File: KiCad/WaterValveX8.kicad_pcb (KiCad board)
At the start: 2 copper layers, 63.2 x 39.1 mm, 50 parts, among them J1 Conn_01x04_Male, J2 Barrel_Jack, J3 Conn_01x03_Male, J4 Conn_01x01_Male, J5 Conn_01x04_Male, J6 Screw_Terminal_01x03, J7 Screw_Terminal_01x03, J8 Screw_Terminal_01x03, J9 Screw_Terminal_01x02, Q1 IRLML2502, Q2 IRLML2502, Q3 IRLML2502, Q4 IRLML2502, U1 Project_DCDC_01, U2 SeedStudio XIAO ESP32 C3 v1, U3 L7805

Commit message: First X8 layout
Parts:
- removed J1: Conn_01x04_Male, Connector_PinHeader_2.54mm:PinHeader_1x04_P2.54mm_Vertical
- removed U1: Project_DCDC_01, LOCAL1:DCDC_01
- added D13: LED, LED_SMD:LED_0805_2012Metric_Pad1.15x1.40mm_HandSolder, F.Cu at (186.5, 86.6)
- added D14: LED, LED_THT:LED_D3.0mm, B.Cu at (177.8, 94.0)
- added D15: LED, LED_THT:LED_D3.0mm, B.Cu at (192.8, 113.2)
- added D16: LED, LED_THT:LED_D3.0mm, B.Cu at (192.8, 108.0)
- added D17: LED, LED_THT:LED_D3.0mm, B.Cu at (192.9, 102.5)
- added D18: LED, LED_THT:LED_D3.0mm, B.Cu at (192.8, 96.8)
- added D19: LED, LED_THT:LED_D3.0mm, B.Cu at (152.4, 112.5)
- added D20: LED, LED_SMD:LED_0805_2012Metric_Pad1.15x1.40mm_HandSolder, F.Cu at (151.1, 112.5)
- added D21: 1N4148, Diode_SMD:D_MiniMELF, F.Cu at (147.2, 113.0)
- added D22: LED, LED_THT:LED_D3.0mm, B.Cu at (152.4, 106.4)
- added D23: LED, LED_SMD:LED_0805_2012Metric_Pad1.15x1.40mm_HandSolder, F.Cu at (151.1, 106.4)
- added D24: 1N4148, Diode_SMD:D_MiniMELF, F.Cu at (147.2, 107.0)
- added D25: LED, LED_THT:LED_D3.0mm, B.Cu at (152.4, 100.6)
- added D26: LED, LED_SMD:LED_0805_2012Metric_Pad1.15x1.40mm_HandSolder, F.Cu at (151.1, 100.6)
- added D27: 1N4148, Diode_SMD:D_MiniMELF, F.Cu at (147.2, 101.0)
- added D28: LED, LED_THT:LED_D3.0mm, B.Cu at (152.4, 94.7)
- added D29: LED, LED_SMD:LED_0805_2012Metric_Pad1.15x1.40mm_HandSolder, F.Cu at (151.1, 94.7)
- added D30: 1N4148, Diode_SMD:D_MiniMELF, F.Cu at (147.2, 95.2)
- added J10: Screw_Terminal_01x03, TerminalBlock_Phoenix:TerminalBlock_Phoenix_PT-1,5-3-3.5-H_1x03_P3.50mm_Horizontal, F.Cu at (142.3, 106.8)
- added J11: Conn_01x03_Pin, Connector_PinHeader_2.54mm:PinHeader_1x03_P2.54mm_Vertical, F.Cu at (147.5, 90.0)
- added Q5: IRLML2502, Package_TO_SOT_SMD:SOT-23_Handsoldering, F.Cu at (156.5, 115.6)
- added Q6: IRLML2502, Package_TO_SOT_SMD:SOT-23_Handsoldering, F.Cu at (156.5, 109.5)
- added Q7: IRLML2502, Package_TO_SOT_SMD:SOT-23_Handsoldering, F.Cu at (156.5, 103.4)
- added Q8: IRLML2502, Package_TO_SOT_SMD:SOT-23_Handsoldering, F.Cu at (156.5, 97.5)
- added R14: 1k, Resistor_SMD:R_0805_2012Metric_Pad1.20x1.40mm_HandSolder, F.Cu at (160.5, 115.6)
- added R17: 1k, Resistor_SMD:R_0805_2012Metric_Pad1.20x1.40mm_HandSolder, F.Cu at (155.7, 112.5)
- added R18: 1k, Resistor_SMD:R_0805_2012Metric_Pad1.20x1.40mm_HandSolder, F.Cu at (160.5, 109.5)
- added R19: 1k, Resistor_SMD:R_0805_2012Metric_Pad1.20x1.40mm_HandSolder, F.Cu at (155.7, 106.4)
- added R20: 1k, Resistor_SMD:R_0805_2012Metric_Pad1.20x1.40mm_HandSolder, F.Cu at (160.5, 103.5)
- added R21: 1k, Resistor_SMD:R_0805_2012Metric_Pad1.20x1.40mm_HandSolder, F.Cu at (155.7, 100.3)
- added R22: 1k, Resistor_SMD:R_0805_2012Metric_Pad1.20x1.40mm_HandSolder, F.Cu at (160.5, 97.5)
- added R23: 1k, Resistor_SMD:R_0805_2012Metric_Pad1.20x1.40mm_HandSolder, F.Cu at (155.7, 94.7)
- C1, C3: footprint Capacitor_Tantalum_SMD:CP_EIA-3216-18_Kemet-A_Pad1.58x1.35mm_HandSolder -> Capacitor_SMD:C_1206_3216Metric_Pad1.33x1.80mm_HandSolder
- D10, D3, D5, D8: moved to F.Cu
- D11: footprint LED_SMD:LED_0805_2012Metric_Pad1.15x1.40mm_HandSolder -> LED_THT:LED_D3.0mm; moved to B.Cu
- D12, D4, D6, D9: value 1N4007 -> 1N4148; footprint Diode_THT:D_DO-41_SOD81_P3.81mm_Vertical_KathodeUp -> Diode_SMD:D_MiniMELF
- J2: value Barrel_Jack -> Screw_Terminal_01x03; footprint LOCAL1:BarrelJack1 -> TerminalBlock_Phoenix:TerminalBlock_Phoenix_PT-1,5-3-3.5-H_1x03_P3.50mm_Horizontal
- U2: value SeedStudio XIAO ESP32 C3 v1 -> XIAO-ESP32-C6-SMD; footprint LOCAL1:XIAO_ESP32C3_THT -> LOCAL1:XIAO-ESP32-C6-SMD
- moved J9 32.6 mm to (160.2, 90.1), turned to 180 degrees
- moved J5 26.9 mm to (154.8, 119.2), turned to -90 degrees
- moved R5 24.2 mm to (151.0, 116.5), turned to 0 degrees
- moved R4 19.1 mm to (159.0, 119.2), turned to 180 degrees
- moved C2 15.7 mm to (166.1, 95.8)
- moved D12 14.0 mm to (198.0, 97.2), turned to -90 degrees
- moved C1 13.8 mm to (163.8, 95.2), turned to -90 degrees
- moved D9 13.7 mm to (197.9, 102.8), turned to -90 degrees
- moved D4 13.6 mm to (198.0, 114.2), turned to -90 degrees
- moved D6 13.5 mm to (197.9, 108.5), turned to -90 degrees
- moved J2 13.1 mm to (142.2, 95.0), turned to -90 degrees
- moved D10 12.8 mm to (193.8, 96.8), turned to 0 degrees
- moved D8 12.7 mm to (194.1, 102.5), turned to 0 degrees
- moved D11 12.6 mm to (187.7, 86.6)
- moved D5 12.4 mm to (194.0, 108.0), turned to 0 degrees
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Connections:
- D7 pad 2: /GPIO10 -> /D10
- J2 pad 1: /PwrIn -> +VSW
- J2 pad 2: GND -> /Relay8
- J2 pad 3: unconnected-(J2-Pad3) -> /Relay7
- R11 pad 1: /GPIO8 -> /D8
- R12 pad 2: /GPIO10 -> /D10
- R6 pad 1: /GPIO1 -> /D1
- R8 pad 1: /GPIO5 -> /D2
- R9 pad 1: /GPIO3 -> /D3
- U2 pad 1: /GPIO2 -> +5V
- U2 pad 10: Net-(D1-K) -> /SDA
- U2 pad 11: /GPIO10 -> /D3
- U2 pad 12: +3V3 -> /D2
- U2 pad 13: GND -> /D1
- U2 pad 14: +5V -> /GPIO2
- U2 pad 2: /GPIO1 -> GND
- U2 pad 3: /GPIO5 -> +3V3
- U2 pad 4: /GPIO3 -> /D10
- U2 pad 5: /SDA -> Net-(D1-K)
- U2 pad 6: /SCL -> /D8
- U2 pad 7: /TX -> /RX
- U2 pad 8: /RX -> /TX
- U2 pad 9: /GPIO8 -> /SCL
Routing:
- net +VSW: track 56.3 -> 148.1 mm
- net GND: track 0.00 -> 85.4 mm, vias 3 -> 12
- net /RX: track 3.25 -> 43.4 mm, vias 0 -> 2
- net /GPIO10: track 30.0 -> 0.00 mm, vias 1 -> 0
- net /PwrIn: track 55.8 -> 28.9 mm
- net /D3: track 0.00 -> 25.7 mm, vias 0 -> 2
- net /D1: track 0.00 -> 23.4 mm, vias 0 -> 2
- net /D2: track 0.00 -> 23.0 mm, vias 0 -> 2
- net +5V: track 85.6 -> 63.5 mm, vias 0 -> 1
- net /GPIO8: track 21.3 -> 0.00 mm, vias 1 -> 0
- net /D10: track 0.00 -> 19.9 mm, vias 0 -> 2
- net /Relay6: track 0.00 -> 19.2 mm
- net /Relay5: track 0.00 -> 18.3 mm
- net /Relay7: track 0.00 -> 16.9 mm
- net /Relay8: track 0.00 -> 16.8 mm
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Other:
- board size 63.2 x 39.1 mm -> 72.9 x 41.6 mm
- board text added: "(C) 2025 Hans Rune Bue <email@hansrune.net>"
- board text added: "GND 3V DA CL"
- board text added: "RX TX GND"
- board text added: "WaterValveX8 - Rev 4.0"
- board text removed: "(C) 2023 Hans Rune Bue <email@hansrune.net>"
- board text removed: "CL DA +3V GND"
- board text removed: "WaterValveX4 - Rev 2.0.1"

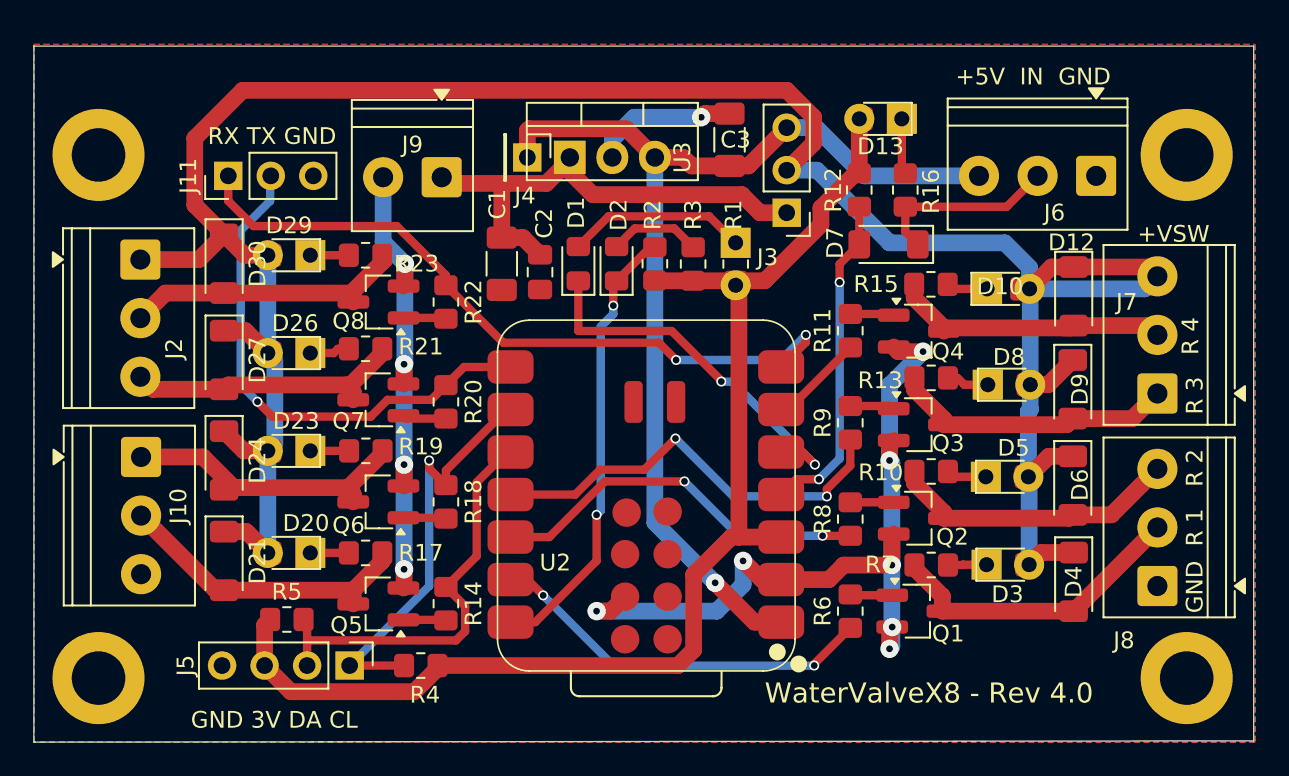
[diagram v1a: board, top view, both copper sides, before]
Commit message: Diode footprint changes
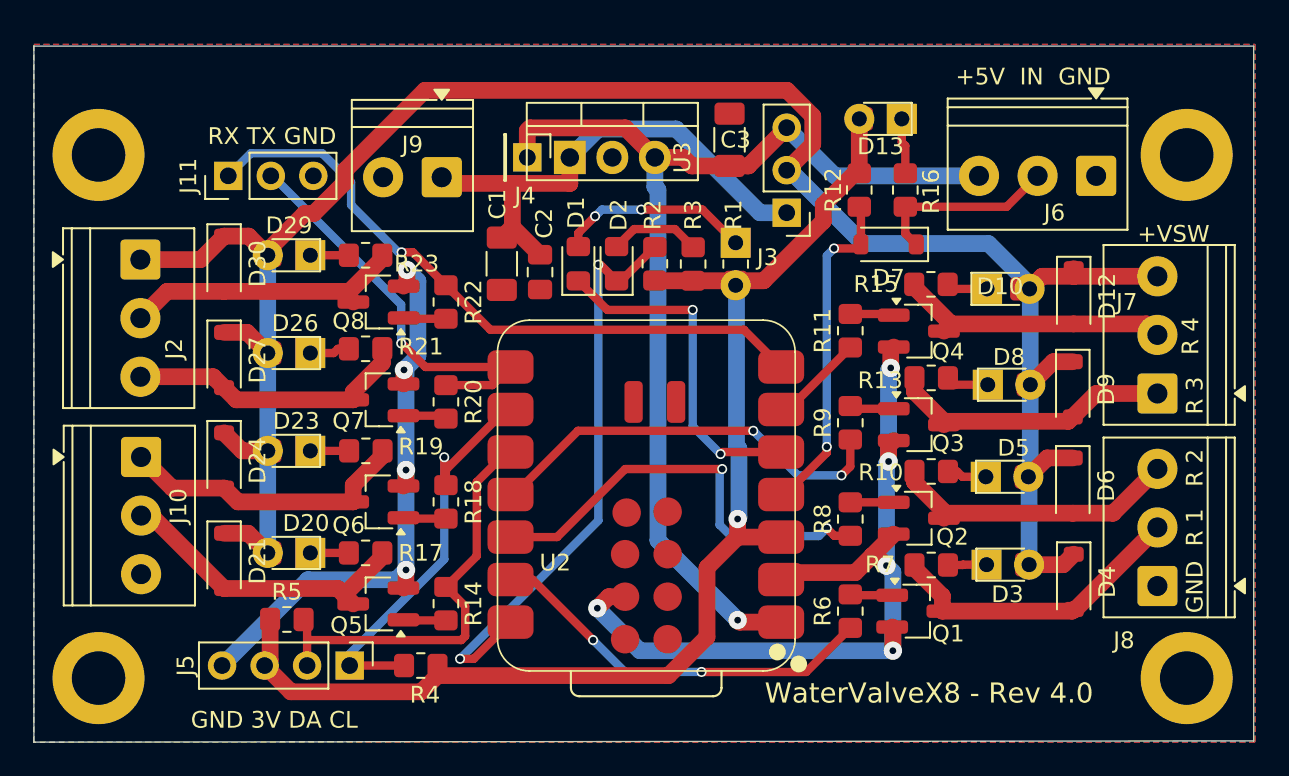
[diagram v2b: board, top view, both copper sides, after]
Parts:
- D12, D21, D24, D27, D30, D4, D6, D7, D9: footprint Diode_SMD:D_MiniMELF -> Diode_SMD:D_SOD-123
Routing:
- net +VSW: track 148.1 -> 131.4 mm
- net /GPIO2: track 27.0 -> 35.5 mm
- net /TX: track 31.4 -> 24.7 mm
- net /RX: track 43.4 -> 39.7 mm, vias 2 -> 1
- net /D2: track 23.0 -> 26.2 mm
- net Net-(D1-K): track 22.8 -> 20.5 mm
- net /PwrIn: track 28.9 -> 30.9 mm
- net GND: track 85.4 -> 87.1 mm, vias 12 -> 9
- net /Relay6: track 19.2 -> 17.6 mm
- net /D3: track 25.7 -> 24.8 mm
- net Net-(D1-A): track 11.1 -> 11.9 mm, vias 0 -> 2
- net +5V: track 63.5 -> 64.1 mm
- net +3V3: vias 0 -> 1

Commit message: Changed to combined C3/C6 and step-down PSU
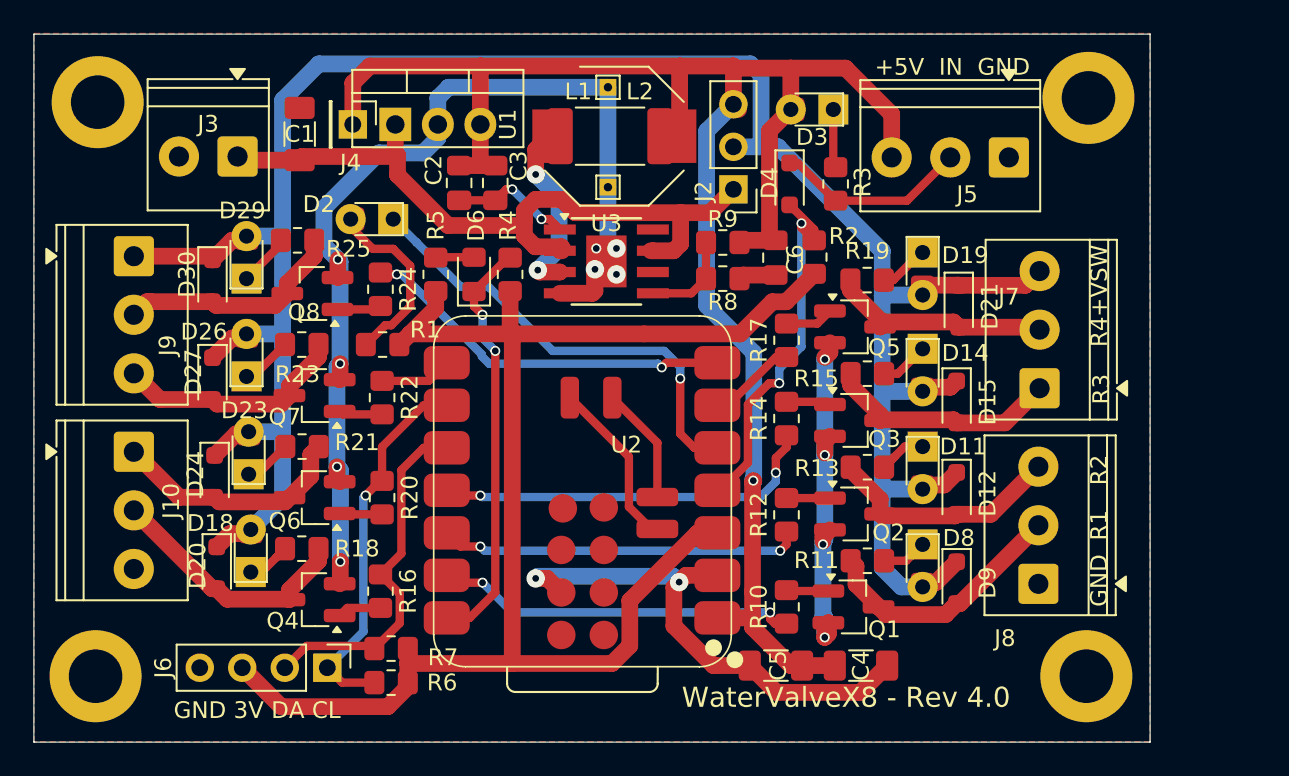
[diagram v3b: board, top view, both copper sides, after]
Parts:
- removed J11: Conn_01x03_Pin, Connector_PinHeader_2.54mm:PinHeader_1x03_P2.54mm_Vertical
- added C4: 22uF, Capacitor_SMD:C_1206_3216Metric_Pad1.33x1.80mm_HandSolder, F.Cu at (185.3, 119.3)
- added C5: 22uF, Capacitor_SMD:C_1206_3216Metric_Pad1.33x1.80mm_HandSolder, F.Cu at (180.2, 119.3)
- added C6: 100nF, Capacitor_SMD:C_0805_2012Metric_Pad1.18x1.45mm_HandSolder, F.Cu at (180.2, 94.9)
- added L1: L, Inductor_SMD:L_Bourns-SRU8028_8.0x8.0mm, F.Cu at (170.6, 87.6)
- added L2: L, Inductor_SMD:L_2512_6332Metric_Pad1.52x3.35mm_HandSolder, F.Cu at (170.3, 87.6)
- added R8: 88k7, Resistor_SMD:R_0805_2012Metric_Pad1.20x1.40mm_HandSolder, F.Cu at (177.0, 94.0)
- added R9: 20k, Resistor_SMD:R_0805_2012Metric_Pad1.20x1.40mm_HandSolder, F.Cu at (177.0, 96.1)
- added TP1: TestPoint, TestPoint:TestPoint_THTPad_1.0x1.0mm_Drill0.5mm, F.Cu at (170.2, 84.7)
- added TP2: TestPoint, TestPoint:TestPoint_THTPad_1.0x1.0mm_Drill0.5mm, F.Cu at (170.2, 90.7)
- added U3: MT2499A, Package_SO:TI_SO-PowerPAD-8, F.Cu at (170.1, 95.1)
- C1: value 10uF -> 22uF
- C3: value 10uF -> 22nF; footprint Capacitor_SMD:C_1206_3216Metric_Pad1.33x1.80mm_HandSolder -> Capacitor_SMD:C_0805_2012Metric_Pad1.18x1.45mm_HandSolder
- D12: renamed from D6; value 1N4148 -> 1N4007; footprint Diode_SMD:D_SOD-123 -> Diode_SMD:D_SOD-323_HandSoldering
- D15: renamed from D9; value 1N4148 -> 1N4007; footprint Diode_SMD:D_SOD-123 -> Diode_SMD:D_SOD-323_HandSoldering
- D20: renamed from D21; value 1N4148 -> 1N4007; footprint Diode_SMD:D_SOD-123 -> Diode_SMD:D_SOD-323_HandSoldering
- D21: renamed from D12; value 1N4148 -> 1N4007; footprint Diode_SMD:D_SOD-123 -> Diode_SMD:D_SOD-323_HandSoldering
- D24, D27, D30: value 1N4148 -> 1N4007; footprint Diode_SMD:D_SOD-123 -> Diode_SMD:D_SOD-323_HandSoldering
- D4: renamed from D7; value 1N4148 -> D; footprint Diode_SMD:D_SOD-123 -> Diode_SMD:D_SOD-323_HandSoldering
- D9: renamed from D4; value 1N4148 -> 1N4007; footprint Diode_SMD:D_SOD-123 -> Diode_SMD:D_SOD-323_HandSoldering
- U2: footprint LOCAL1:XIAO-ESP32-C6-SMD -> LOCAL1:XIAO-ESP32-C3C6-SMD
- moved R1 21.6 mm to (156.7, 100.1), turned to 0 degrees
- moved D1 20.5 mm to (157.4, 92.6), turned to 180 degrees
- moved R5 15.4 mm to (159.9, 95.9)
- moved C1 14.3 mm to (151.8, 87.5), turned to 90 degrees
- moved C3 14.2 mm to (163.4, 90.4)
- moved D2 12.6 mm to (156.1, 92.6), turned to 180 degrees
- moved J3 12.3 mm to (148.1, 88.8)
- moved J4 10.6 mm to (154.9, 86.9)
- moved U1 10.6 mm to (157.5, 86.9)
- moved R4 8.67 mm to (164.3, 95.9)
- moved D6 8.54 mm to (162.2, 95.9)
- moved C2 7.19 mm to (161.3, 90.4), turned to 90 degrees
- moved J8 7.11 mm to (195.9, 114.4)
- moved J7 7.05 mm to (196.0, 102.7)
- moved D9 6.99 mm to (191.0, 114.3)
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- renumbered D14 to D1, D16 to D10, D5 to D11, D17 to D13, D8 to D14, D19 to D16, D18 to D17, D20 to D18, D10 to D19, D1 to D2, D13 to D3, D11 to D5, D2 to D6, D15 to D7, D3 to D8, H5 to H1, H6 to H2, H7 to H3, H8 to H4, J3 to J2, J9 to J3, J6 to J5, J5 to J6, J2 to J9, Q5 to Q4, Q4 to Q5, R6 to R10, R7 to R11, R8 to R12, R10 to R13, R9 to R14, R13 to R15, R14 to R16, R11 to R17, R17 to R18, R15 to R19, R12 to R2, R18 to R20, R19 to R21, R20 to R22, R21 to R23, R22 to R24, R23 to R25, R16 to R3, R2 to R4, R3 to R5, R4 to R6, R5 to R7, U3 to U1
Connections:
- net /RX renamed Net-(U2-GPIO16_D6_TX)
- net /TX renamed Net-(U2-GPIO17_D7_RX)
- C1 pad 1: /PwrIn -> /Vin
- C2 pad 1: /PwrIn -> Net-(U3-BS)
- C2 pad 2: GND -> +5V
- C3 pad 1: +5V -> Net-(U3-BS)
- C3 pad 2: GND -> +5V
- D1 pad 1: Net-(D1-A) -> Net-(D1-K)
- D1 pad 2: +3V3 -> Net-(D1-A)
- D3 pad 2: +3V3 -> +5V
- D5 pad 2: +3V3 -> +5V
- J2 pad 1: /PwrIn -> /Vin
- J3 pad 1: /PwrIn -> /Vin
- U1 pad 1: /PwrIn -> /Vin
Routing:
- net +5V: track 64.1 -> 110.0 mm
- net /Vin: track 0.00 -> 44.6 mm
- net /PwrIn: track 30.9 -> 0.00 mm
- net GND: track 87.1 -> 115.5 mm, vias 9 -> 14
- net Net-(U2-GPIO17_D7_RX): track 24.7 -> 4.31 mm, vias 1 -> 0
- net Net-(U2-GPIO16_D6_TX): track 39.7 -> 23.1 mm, vias 1 -> 2
- net +3V3: track 75.6 -> 90.4 mm, vias 1 -> 0
- net /IND1: track 0.00 -> 11.5 mm, vias 0 -> 2
- net unconnected-(U2-GND-Pad16): track 0.00 -> 10.2 mm
- net /GPIO2: track 35.5 -> 25.7 mm
- net +VSW: track 131.4 -> 140.0 mm
- net Net-(U3-BS): track 0.00 -> 7.74 mm, vias 0 -> 2
- net Net-(D1-K): track 20.5 -> 27.6 mm, vias 2 -> 1
- net unconnected-(U2-BAT-Pad15): track 0.00 -> 7.05 mm
- net Net-(U3-FB): track 0.00 -> 5.70 mm
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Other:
- board size 72.9 x 41.6 mm -> 66.7 x 42.3 mm
- board text added: "R1"
- board text added: "R2"
- board text added: "R3"
- board text added: "R4"
- board text removed: "R 1"
- board text removed: "R 2"
- board text removed: "R 3"
- board text removed: "R 4"
- board text removed: "RX TX GND"
